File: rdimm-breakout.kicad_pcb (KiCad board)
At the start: 10 copper layers, 152.9 x 45 mm, 89 parts, among them IC1 TPS54561, J3 DC_SOCKET, U14 2199155-1, U2 TPS65295RJET, U8 PCA9517ADMR2G

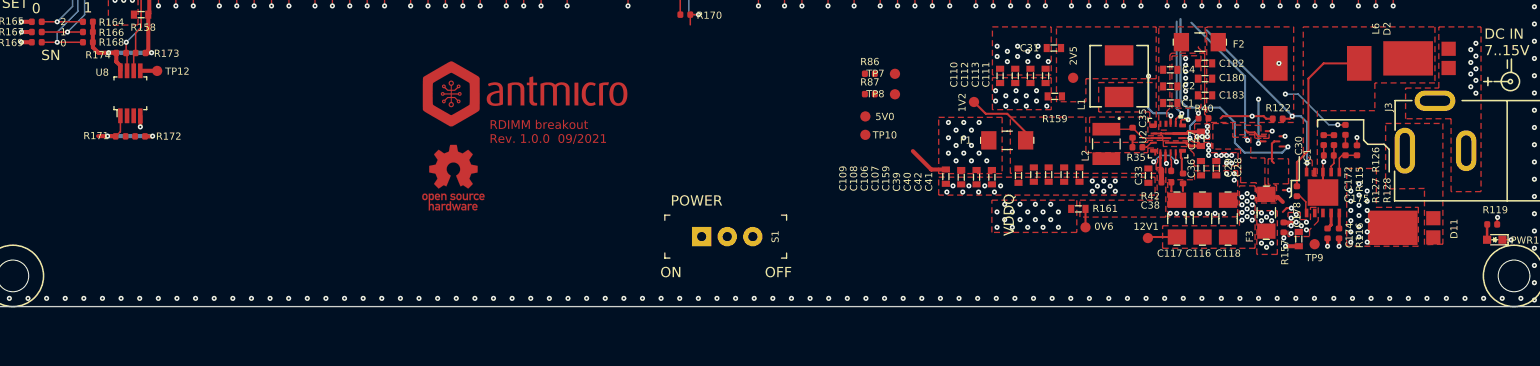
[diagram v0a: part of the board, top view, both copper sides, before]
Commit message: Add I2C connector
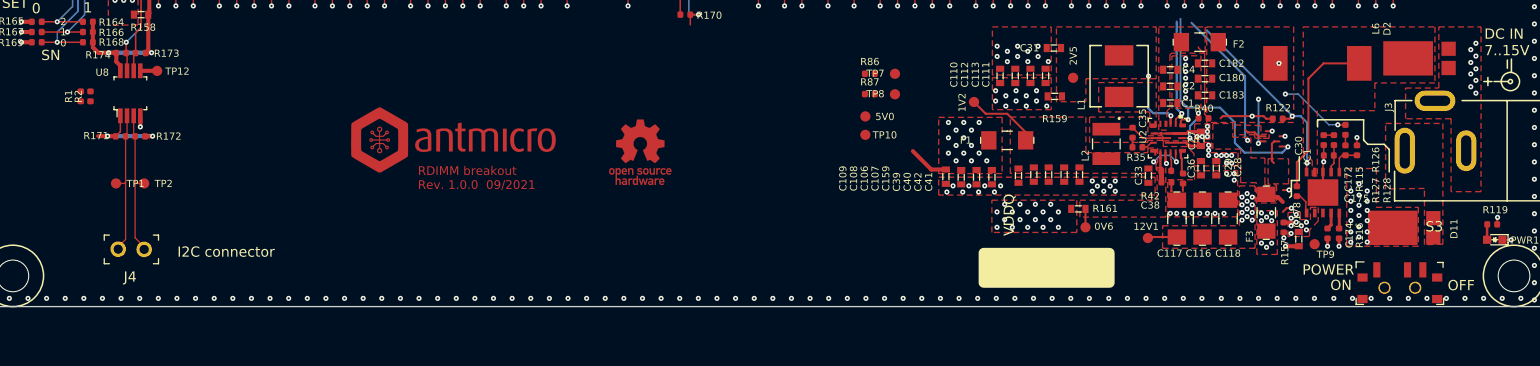
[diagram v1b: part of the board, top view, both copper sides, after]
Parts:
- removed S1: EG1218, rdimm-breakout-footprints:Switch_Slide_11.6x4mm_EG1218
- added J4: 61300211121, rdimm-breakout-footprints:PinHeader_1x2_P2.54_Drill0.9mm, F.Cu at (122.8, 85.4)
- added R1: R_0R_0402, rdimm-breakout-footprints:0402-res, F.Cu at (116.6, 70.5)
- added R2: R_0R_0402, rdimm-breakout-footprints:0402-res, F.Cu at (117.6, 70.5)
- added S3: MSS3-V-T_R, rdimm-breakout-footprints:Switch_Slide_MSS3, F.Cu at (245.6, 89.2)
- added TP1: TP_SMD1MM, rdimm-breakout-footprints:Testpoint_smd_1mm, F.Cu at (120.1, 78.9)
- added TP2: TP_SMD1MM, rdimm-breakout-footprints:Testpoint_smd_1mm, F.Cu at (122.8, 78.9)
- moved N1 18.4 mm to (171.3, 75.9)
- moved N2 8.32 mm to (153.1, 74.9)
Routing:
- net SDA_1V2: track 0.00 -> 14.2 mm
- net SCL_1V2: track 0.00 -> 14.2 mm
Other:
- board text added: "I2C connector"

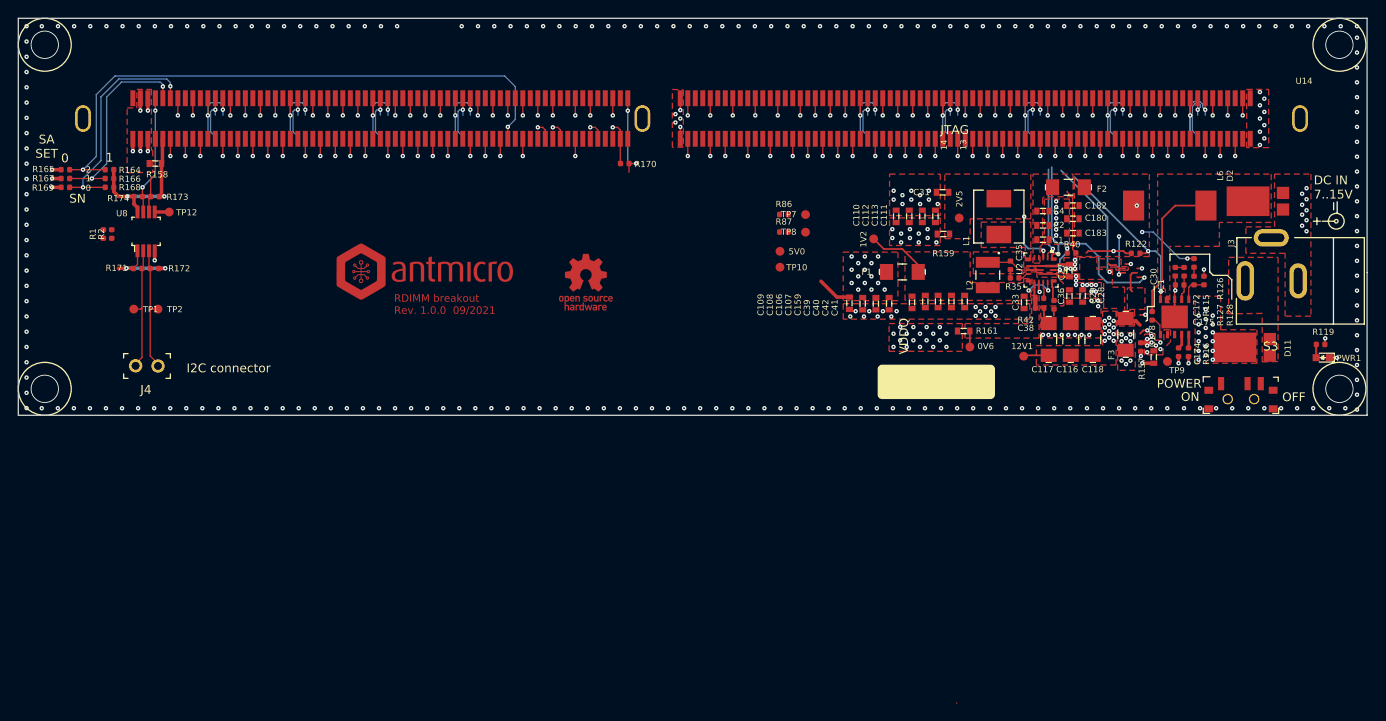
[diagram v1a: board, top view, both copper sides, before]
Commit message: Add initial component placement
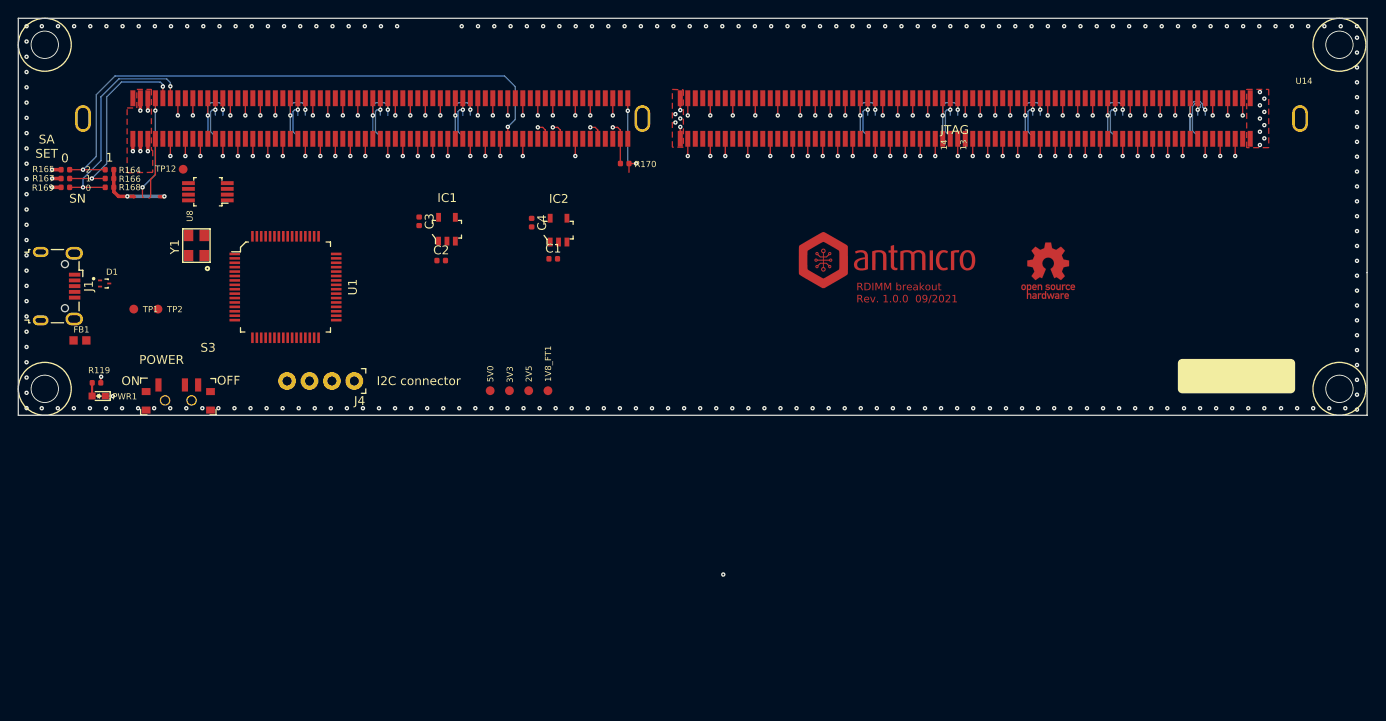
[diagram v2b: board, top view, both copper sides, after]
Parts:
- removed 0V6, 1V2, TP10, TP7, TP8, TP9: TP_SMD1MM, rdimm-breakout-footprints:Testpoint_smd_1mm
- removed C106, C107, C108, C109, C110, C111, C112, C113: C_10n_0603, rdimm-breakout-footprints:0603-cap
- removed C116, C117, C118: C_47u_16V_1206, rdimm-breakout-footprints:1206-cap
- removed C159, C31, C39, C40, C41, C42: C_22u_0603, rdimm-breakout-footprints:0603-cap
- removed C172: C_4n7_0402, rdimm-breakout-footprints:0402-cap
- removed C174: C_10n_0402, rdimm-breakout-footprints:0402-cap
- removed C175: C_47p_0402, rdimm-breakout-footprints:0402-cap
- removed C178, C35: C_100n_0402_6V3, rdimm-breakout-footprints:0402-cap
- removed C180, C182, C183: C_47u_0603, rdimm-breakout-footprints:0603-cap
- removed C27, C28, C29: C_10u_25V_0603, rdimm-breakout-footprints:0603-cap
- removed C30: C_100n_0402_16V, rdimm-breakout-footprints:0402-cap
- removed C33: C_10u_0603, rdimm-breakout-footprints:0603-cap
- removed C36: C_470n_0402, rdimm-breakout-footprints:0402-cap
- removed C38: C_10u_0402, rdimm-breakout-footprints:0402-cap
- removed D11, D2: PDS760-13, rdimm-breakout-footprints:PDS760-13
- removed F1, F2, F3: 1206L450SLWR, rdimm-breakout-footprints:1206-res
- removed J3: DC_SOCKET, rdimm-breakout-footprints:DC_SOCKET
- removed L1: IHLP2020BZER4R7M01, rdimm-breakout-footprints:IHLP2020BZER4R7M01
- removed L2: DFE322512F-R68M=P2, rdimm-breakout-footprints:INDC3225X120N
- removed L6: WE_7447798720, rdimm-breakout-footprints:WE_7447798720
- removed R1, R2, R42: R_0R_0402, rdimm-breakout-footprints:0402-res
- removed R115: R_16k9_0402, rdimm-breakout-footprints:0402-res
- removed R116: R_243k_0402, rdimm-breakout-footprints:0402-res
- removed R122, R40: R_100k_0402, rdimm-breakout-footprints:0402-res
- removed R126: R_49R9_0402, rdimm-breakout-footprints:0402-res
- removed R127: R_53k6_0402, rdimm-breakout-footprints:0402-res
- removed R128: R_10k2_0402, rdimm-breakout-footprints:0402-res
- removed R157, R158, R159, R161: R_0R_0603, rdimm-breakout-footprints:0603-res
- removed R171, R172, R173, R174: R_4k7_0402, rdimm-breakout-footprints:0402-res
- removed R35: R_5R1_0402, rdimm-breakout-footprints:0402-res
- removed R86, R87: R_10k_0402, rdimm-breakout-footprints:0402-res
- removed U2: TPS65295RJET, rdimm-breakout-footprints:TPS65295RJET
- added 1V8_FT1: TP_SMD1MM, rdimm-breakout-footprints:Testpoint_smd_1mm, F.Cu at (167.0, 88.2)
- added C3: C_1u_0402, rdimm-breakout-footprints:0402-cap, F.Cu at (152.4, 69.0)
- added D1: PESD5V0S2BQA, rdimm-breakout-footprints:TPD2E009DRTR, F.Cu at (116.8, 76.1)
- added FB1: BLM18AG601SN1D, rdimm-breakout-footprints:0603, F.Cu at (114.0, 82.5)
- added IC2: MIC5225-3.3YM5-TR, rdimm-breakout-footprints:SOT-23-5, F.Cu at (168.2, 70.0)
- added J1: WE_629105150521, rdimm-breakout-footprints:USB_Micro_B_Female_629105150521, F.Cu at (111.5, 76.4)
- added U1: FT2232HL-REEL, antmicro-footprints:LQFP-64_10x10mm, F.Cu at (137.3, 76.5)
- added Y1: KX-7_12,MHz, rdimm-breakout-footprints:KX-7, F.Cu at (127.1, 71.8)
- C1: value C_10u_0603 -> C_1u_0402; footprint rdimm-breakout-footprints:0603-cap -> rdimm-breakout-footprints:0402-cap
- C2: value C_100n_0603 -> C_1u_0402; footprint rdimm-breakout-footprints:0603-cap -> rdimm-breakout-footprints:0402-cap
- C4: value C_1u_0603 -> C_1u_0402; footprint rdimm-breakout-footprints:0603-cap -> rdimm-breakout-footprints:0402-cap
- IC1: value TPS54561 -> MIC5317-2.5YM5-TR; footprint rdimm-breakout-footprints:WSON-10_4x4 -> rdimm-breakout-footprints:SOT-23-5
- J4: value 61300211121 -> 0022232041; footprint rdimm-breakout-footprints:PinHeader_1x2_P2.54_Drill0.9mm -> antmicro-footprints:PinHeader_1x4_P2.54mm_Drill1.02mm
- moved PWR1 138.8 mm to (116.1, 88.8)
- moved R119 138.8 mm to (115.9, 87.3)
- moved S3 120.5 mm to (125.1, 89.3)
- moved IC1 83.1 mm to (155.6, 69.9), turned to 0 degrees
- moved C2 68.3 mm to (154.9, 73.5)
- moved 3V3 58.5 mm to (162.6, 88.2), turned to 270 degrees
- moved C4 58.0 mm to (165.2, 69.2), turned to 270 degrees
- moved C1 55.5 mm to (167.6, 73.3)
- moved 2V5 52.6 mm to (164.8, 88.2)
- moved N2 52.4 mm to (205.5, 73.6)
- moved N1 52.4 mm to (223.7, 74.6)
- moved 5V0 36.5 mm to (160.4, 88.2), turned to 270 degrees
- moved J4 22.3 mm to (145.1, 87.1)
- moved U8 8.32 mm to (128.5, 65.7), turned to 90 degrees
- moved TP12 5.20 mm to (125.7, 63.1), turned to 180 degrees
- renumbered 12V1 to 3V3
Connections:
- net SCL_1V2 renamed SCL
- 3V3 pad 1: VIN -> VCC3V3
- C1 pad 1: 5V0_SYS -> VCC5V0
- C2 pad 1: 5V0_SYS -> VCC3V3
- C4 pad 1: 5V0_SYS -> VCC3V3
- IC1 pad 1: Net-(C178-Pad2) -> VCC3V3
- IC1 pad 2: VIN -> GND
- IC1 pad 3: /Supply/SYS_EN -> VCC3V3
- IC1 pad 4: Net-(C174-Pad1) -> (no net)
- IC1 pad 5: Net-(IC1-Pad5) -> VCC2V5
- J4 pad 1: SDA_1V2 -> V_AUX
- PWR1 pad 1: 3V3_SYS -> VCC3V3
- R164 pad 1: VDDSPD -> VCC2V5
- R166 pad 1: VDDSPD -> VCC2V5
- R168 pad 1: VDDSPD -> VCC2V5
- R170 pad 1: VDDQ -> VCC2V5
- S3 pad 1: (no net) -> VCC3V3
- S3 pad 2: /Supply/SYS_EN -> /FTDI/3V3_EN
- TP2 pad 1: SDA_1V2 -> SDA
- U14 pad 284: VDDSPD -> VCC2V5
- U8 pad 1: VDDQ -> VCC3V3
- U8 pad 3: SDA_1V2 -> SDA
- U8 pad 8: VDDSPD -> VCC2V5
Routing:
- net /Supply/VCC_IO_EN: track 25.6 -> 0.00 mm, vias 2 -> 0
- net SYS_ON: track 19.5 -> 0.00 mm, vias 2 -> 0
- net GND: track 219.6 -> 200.7 mm, vias 332 -> 262
- net VDDSPD: track 18.4 -> 0.00 mm, vias 2 -> 0
- net VCC5V0: track 17.5 -> 0.00 mm, vias 6 -> 0
- net Net-(C178-Pad1): track 16.6 -> 0.00 mm
- net VCC3V3: track 15.7 -> 0.86 mm, vias 1 -> 4
- net SDA_1V2: track 14.2 -> 0.00 mm
- net SCL: track 14.2 -> 0.00 mm
- net VDDQ: track 53.0 -> 40.0 mm, vias 36 -> 19
- net VDD1V2: track 10.8 -> 0.00 mm, vias 2 -> 0
- net /Supply/VCC_AUX_EN: track 10.5 -> 0.00 mm, vias 1 -> 0
- net 5V0_SYS: track 7.64 -> 0.00 mm
- net Net-(C35-Pad1): track 5.92 -> 0.00 mm
- net VIN: track 5.33 -> 0.00 mm, vias 47 -> 0
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- removed copper zone on F.Cu, net 3V3_SYS
- removed copper zone on F.Cu, net 5V0_SYS
- removed copper zone on F.Cu, net GND
- removed copper zone on F.Cu, net Net-(C178-Pad1)
- removed copper zone on F.Cu, net Net-(C35-Pad1)
- removed copper zone on F.Cu, net Net-(C45-Pad2)
- removed copper zone on F.Cu, net Net-(D11-PadA)
- removed copper zone on F.Cu, net Net-(L1-Pad1)
- removed copper zone on F.Cu, net Net-(L3-Pad1)
- removed copper zone on F.Cu, net VCC0V6
- removed copper zone on F.Cu, net VCC2V5
- removed copper zone on F.Cu, net VCC3V3
- removed copper zone on F.Cu, net VCC5V0
- removed copper zone on F.Cu, net VDD1V2
- removed copper zone on F.Cu, net VDDQ
- removed copper zone on F.Cu, net VIN
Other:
- board text removed: "DC IN 7..15V"
- board text removed: "VDDQ"

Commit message: Add layout
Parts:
- added C10: C_100n_0402, rdimm-breakout-footprints:0402-cap, F.Cu at (132.5, 68.7)
- added C11: C_100n_0402, rdimm-breakout-footprints:0402-cap, F.Cu at (137.8, 67.5)
- added C12: C_4u7_0402, rdimm-breakout-footprints:0402-cap, F.Cu at (137.8, 68.5)
- added C13: C_100n_0402, rdimm-breakout-footprints:0402-cap, F.Cu at (142.0, 71.8)
- added C14: C_100n_0402, rdimm-breakout-footprints:0402-cap, F.Cu at (125.0, 76.2)
- added C15: C_100n_0402, rdimm-breakout-footprints:0402-cap, F.Cu at (124.2, 74.3)
- added C16: C_100n_0402, rdimm-breakout-footprints:0402-cap, F.Cu at (132.8, 83.5)
- added C17: C_4u7_0402, rdimm-breakout-footprints:0402-cap, F.Cu at (125.0, 77.2)
- added C18: C_4u7_0402, rdimm-breakout-footprints:0402-cap, F.Cu at (121.8, 73.8)
- added C19: C_100n_0402, rdimm-breakout-footprints:0402-cap, F.Cu at (137.2, 83.5)
- added C20: C_100n_0402, rdimm-breakout-footprints:0402-cap, F.Cu at (142.0, 74.8)
- added C21: C_100n_0402, rdimm-breakout-footprints:0402-cap, F.Cu at (135.2, 68.5)
- added C22: C_100n_0402, rdimm-breakout-footprints:0402-cap, F.Cu at (130.2, 68.1)
- added C23: C_100n_0402, rdimm-breakout-footprints:0402-cap, F.Cu at (126.8, 68.1)
- added C5: C_100n_0402, rdimm-breakout-footprints:0402-cap, F.Cu at (115.8, 72.9)
- added C6: C_27p_0402, rdimm-breakout-footprints:0402-cap, F.Cu at (121.3, 70.5)
- added C7: C_27p_0402, rdimm-breakout-footprints:0402-cap, F.Cu at (126.9, 70.5)
- added C8: C_100n_0402, rdimm-breakout-footprints:0402-cap, F.Cu at (127.0, 77.2)
- added C9: C_100n_0402, rdimm-breakout-footprints:0402-cap, F.Cu at (142.0, 78.2)
- added FB2: BLM18AG601SN1D, rdimm-breakout-footprints:0603, F.Cu at (124.7, 78.5)
- added FB3: BLM18AG601SN1D, rdimm-breakout-footprints:0603, F.Cu at (119.4, 72.4)
- added R1: R_0R_0603, rdimm-breakout-footprints:0603-res, F.Cu at (150.2, 82.0)
- added R10: R_10k_0402, rdimm-breakout-footprints:0402-res, F.Cu at (124.6, 64.6)
- added R11: R_10k_0402, rdimm-breakout-footprints:0402-res, F.Cu at (124.6, 66.7)
- added R12: R_0R_0603, rdimm-breakout-footprints:0603-res, F.Cu at (143.8, 83.7)
- added R2: R_4k7_0402, rdimm-breakout-footprints:0402-res, F.Cu at (124.4, 80.7)
- added R3: R_10k_0402, rdimm-breakout-footprints:0402-res, F.Cu at (124.4, 81.7)
- added R4: R_12k_0402, rdimm-breakout-footprints:0402-res, F.Cu at (125.7, 74.8)
- added R5: R_0R_0603, rdimm-breakout-footprints:0603-res, F.Cu at (130.4, 84.0)
- added R6: R_0R_0603, rdimm-breakout-footprints:0603-res, F.Cu at (131.7, 86.3)
- added R7: R_220R_0402, rdimm-breakout-footprints:0402-res, F.Cu at (133.1, 86.5)
- added R8: R_10k_0402, rdimm-breakout-footprints:0402-res, F.Cu at (132.5, 66.7)
- added R9: R_10k_0402, rdimm-breakout-footprints:0402-res, F.Cu at (132.5, 64.6)
- moved R170 22.8 mm to (153.0, 64.1)
- moved IC2 17.3 mm to (153.5, 79.0)
- moved C1 17.0 mm to (153.0, 82.0)
- moved C4 14.0 mm to (153.0, 76.0), turned to 0 degrees
- moved TP1 9.21 mm to (127.8, 83.9)
- moved TP2 6.10 mm to (126.2, 84.0), turned to 270 degrees
- moved Y1 3.37 mm to (124.0, 70.5), turned to 0 degrees
- moved U1 2.86 mm to (134.5, 76.0)
- moved IC1 2.09 mm to (153.5, 70.0)
- moved C3 2.09 mm to (153.0, 67.0), turned to 0 degrees
- moved C2 1.99 mm to (153.0, 73.0)
- moved D1 1.65 mm to (118.3, 75.5)
- moved J4 1.47 mm to (143.8, 87.8), turned to 0 degrees
- moved TP12 0.63 mm to (126.3, 62.9)
- moved J1 0.55 mm to (111.5, 75.8)
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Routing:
- net (no net): track 125.3 -> 0.00 mm, vias 72 -> 4
- net 1V8_FT: track 0.00 -> 95.5 mm, vias 0 -> 2
- net GND: track 200.7 -> 271.2 mm, vias 262 -> 357
- net SDA: track 0.00 -> 62.9 mm, vias 0 -> 2
- net SCL: track 0.00 -> 62.5 mm, vias 0 -> 2
- net /FTDI/3V3_EN: track 0.00 -> 34.4 mm, vias 0 -> 2
- net VCC3V3: track 0.86 -> 34.5 mm, vias 4 -> 26
- net ~EVENT: track 10.1 -> 32.4 mm
- net Net-(FB1-Pad1): track 0.00 -> 18.1 mm
- net VCC5V0: track 0.00 -> 16.0 mm, vias 0 -> 1
- net /FTDI/USB_D_N: track 0.00 -> 15.7 mm
- net /FTDI/USB_D_P: track 0.00 -> 15.7 mm
- net OSCI: track 0.00 -> 9.51 mm
- net Net-(C15-Pad1): track 0.00 -> 9.40 mm
- net OSCO: track 0.00 -> 9.21 mm
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- added copper zone on F.Cu, net 1V8_FT
- added copper zone on F.Cu, net GND
- added copper zone on F.Cu, net VBUS
- added copper zone on VCC, net VBUS
- added copper zone on VCC, net VCC2V5
- added copper zone on F.Cu, net VCC3V3
- added copper zone on VCC, net VCC3V3
- added copper zone on B.Cu, net VDDQ
- removed copper zone on VCC2, net 1V0_SYS
- removed copper zone on VCC1, net 1V2_SYS
- removed copper zone on VCC1, net 1V8_FT
- removed copper zone on VCC2, net 1V8_SYS
- removed copper zone on VCC1, net 3V3_SYS
- removed copper zone on GND2, net GND
- removed copper zone on F.Cu, net NC
- removed copper zone on VCC2, net NC
- removed copper zone on VCC2, net VCC5V0
- removed copper zone on VCC1, net VDDQ
- removed copper zone on VCC2, net VIN
- removed copper zone on VCC2, net VPP
- removed copper zone on VCC2, net VTT
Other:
- copper layers 10 -> 4
- rule via_min_size: 0.45 -> 0.4

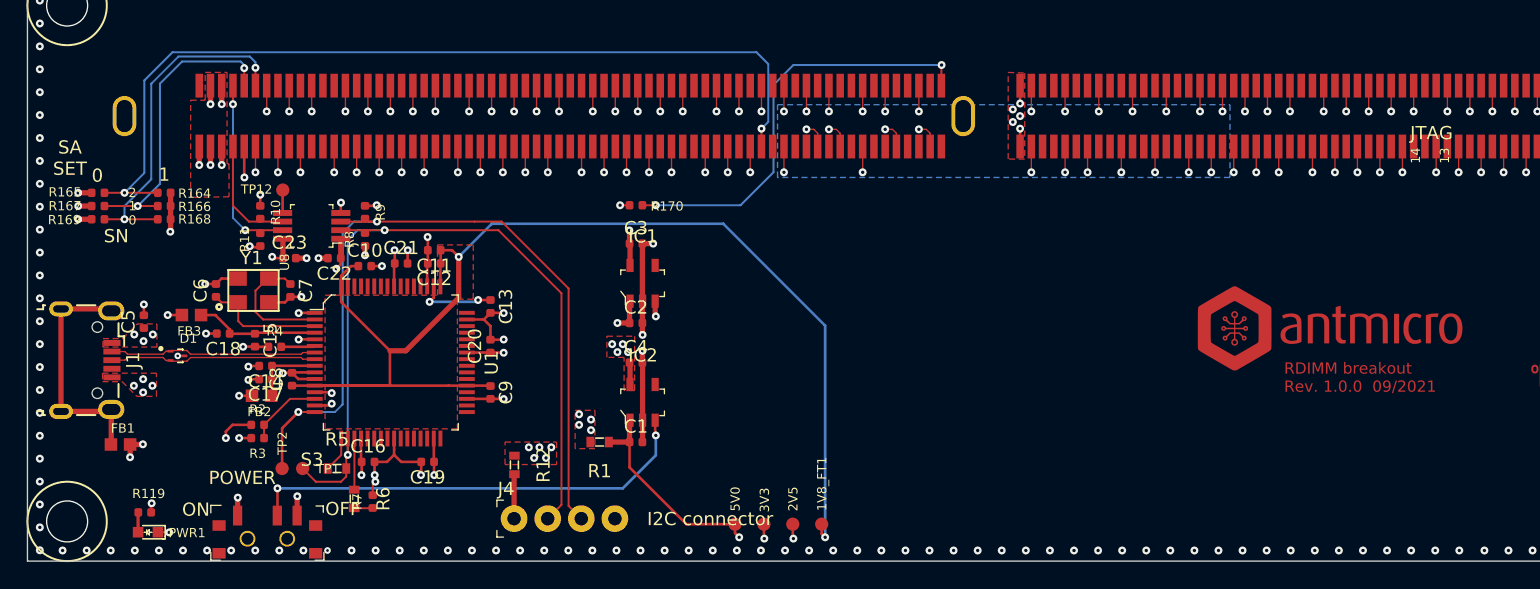
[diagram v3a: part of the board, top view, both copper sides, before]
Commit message: Clean up designators
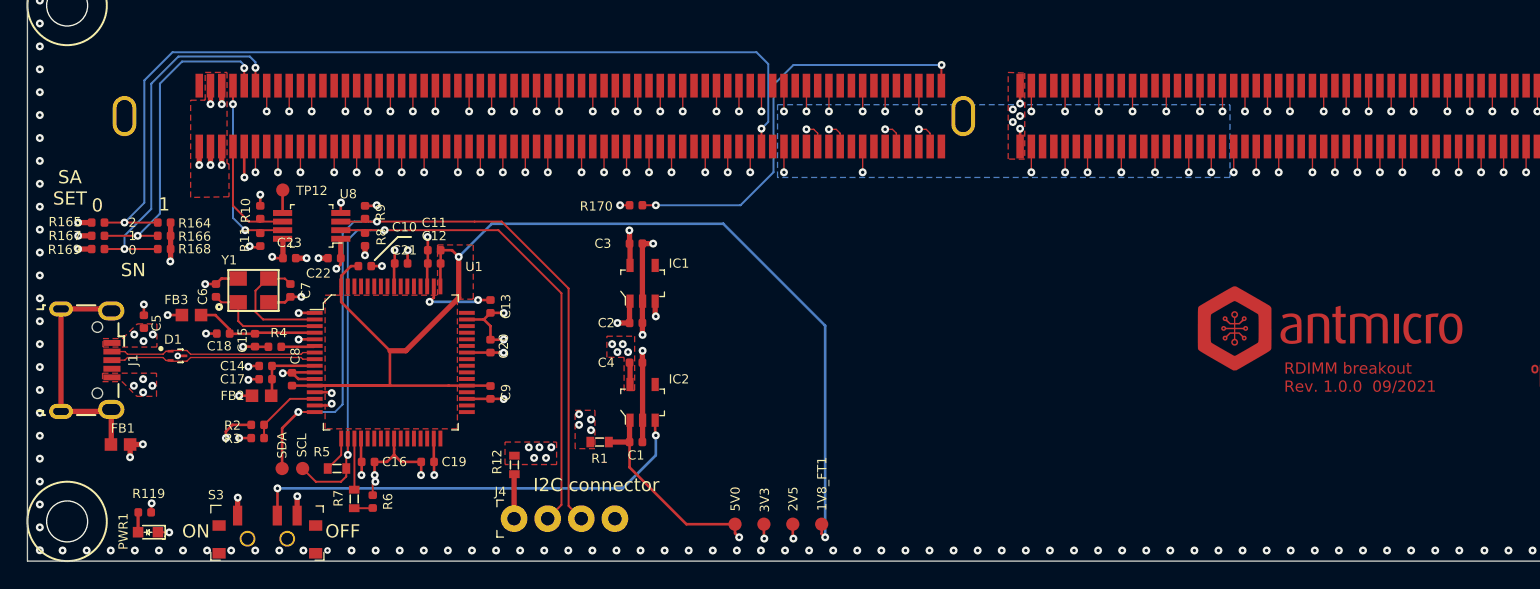
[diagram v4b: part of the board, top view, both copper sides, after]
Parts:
- moved R164 2.25 mm to (117.3, 65.4)
- moved R165 2.25 mm to (112.3, 65.4)
- moved R166 2.25 mm to (117.3, 66.4)
- moved R167 2.25 mm to (112.3, 66.4)
- moved R168 2.25 mm to (117.3, 67.4)
- moved R169 2.25 mm to (112.3, 67.4)
- renumbered TP1 to SCL, TP2 to SDA
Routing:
- net SA2: track 68.0 -> 70.3 mm
- net SA0: track 25.8 -> 28.0 mm
- net SA1: track 22.7 -> 25.0 mm
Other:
- board text removed: "JTAG"
- board text removed: "POWER"
